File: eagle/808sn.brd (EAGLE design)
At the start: 100 x 80 mm, 76 parts, among them IC1 TL072P, IC2 TL072P, Q1 2N3704, Q45 BC546A, Q46 BC556, Q47 BC546A, Q48 BC546A, Q49 BC546A

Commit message: almost routed
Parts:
- moved C6 124.2 mm to (69.6, 71.4)
- moved C3 90.5 mm to (66.0, 51.1)
- moved C4 89.5 mm to (32.3, 64.5)
- moved C5 75.1 mm to (29.2, 43.7), turned to 270 degrees
- moved LEVEL 65.8 mm to (82.5, 3.56), turned to 0 degrees
- moved TONE 58.0 mm to (51.6, 3.56), turned to 0 degrees
- moved R204 47.6 mm to (67.3, 6.60), turned to 90 degrees
- moved C65 46.4 mm to (55.9, 17.5), turned to 270 degrees
- moved C56 45.3 mm to (55.1, 50.0)
- moved R200 43.2 mm to (51.3, 22.6), turned to 180 degrees
- moved C63 42.6 mm to (36.1, 6.60), turned to 270 degrees
- moved TRIGGER 41.5 mm to (12.2, 34.8)
- moved C68 39.4 mm to (88.4, 17.0), turned to 270 degrees
- moved R180 39.0 mm to (9.91, 31.5)
- moved R196 32.7 mm to (25.1, 36.8), turned to 180 degrees
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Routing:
- net GND: track 0.00 -> 329.1 mm
- net N$12: track 0.00 -> 179.2 mm
- net +12V: track 0.00 -> 115.3 mm
- net N$9: track 0.00 -> 101.1 mm
- net N$35: track 0.00 -> 98.7 mm
- net -12V: track 0.00 -> 85.0 mm
- net N$129: track 0.00 -> 81.4 mm
- net N$707: track 0.00 -> 78.6 mm
- net N$29: track 0.00 -> 64.8 mm
- net N$6: track 0.00 -> 41.4 mm
- net N$27: track 0.00 -> 38.6 mm
- net N$8: track 0.00 -> 37.2 mm
- net N$710: track 0.00 -> 34.2 mm
- net N$26: track 0.00 -> 33.0 mm
- net N$15: track 0.00 -> 32.1 mm
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
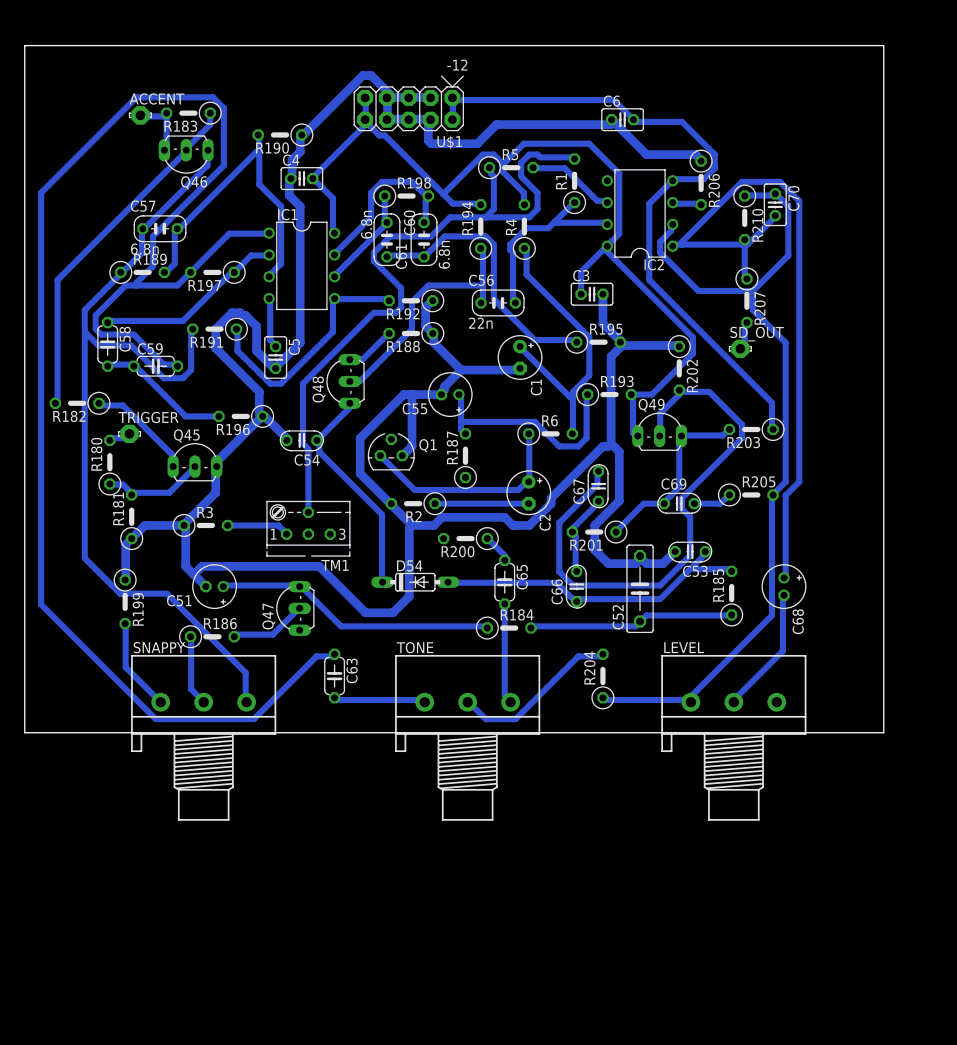
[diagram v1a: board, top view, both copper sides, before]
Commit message: gcode with good separation of traces
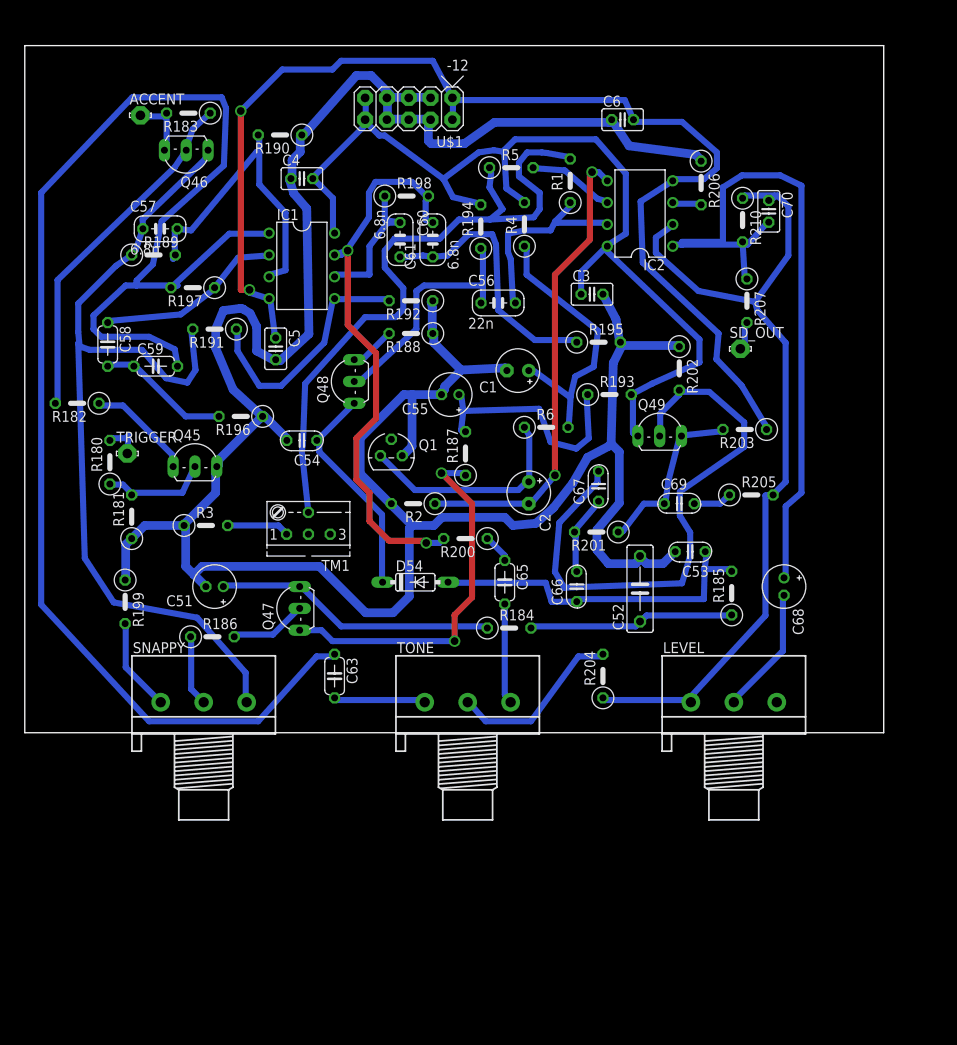
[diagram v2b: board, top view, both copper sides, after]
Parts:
- moved R197 2.90 mm to (19.6, 51.8)
- moved R189 2.40 mm to (15.0, 55.6)
- moved TRIGGER 2.30 mm to (11.9, 32.5)
- moved C1 1.55 mm to (57.4, 42.2), turned to 180 degrees
- moved C60 1.52 mm to (43.7, 57.4)
- moved C70 1.08 mm to (86.6, 60.7)
- moved C5 1.02 mm to (29.2, 44.7)
- moved C61 1.02 mm to (47.5, 57.4)
- moved R6 0.92 mm to (60.7, 35.6)
- moved R203 0.76 mm to (83.8, 35.3)
- moved Q48 0.51 mm to (37.1, 40.9)
- moved R1 0.51 mm to (63.5, 64.3)
- moved R210 0.36 mm to (83.6, 59.7)
- moved R201 0.25 mm to (66.5, 23.4)
- moved R4 0.25 mm to (58.2, 59.2)
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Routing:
- net -12V: track 85.0 -> 140.4 mm, vias 0 -> 2
- net N$14: track 20.1 -> 67.1 mm, vias 0 -> 2
- net N$2: track 10.9 -> 54.8 mm, vias 0 -> 2
- net N$24: track 0.00 -> 43.3 mm, vias 0 -> 2
- net N$160: track 12.1 -> 17.0 mm
- net N$129: track 81.4 -> 85.6 mm
- net N$12: track 179.2 -> 183.1 mm
- net N$29: track 64.8 -> 67.9 mm
- net GND: track 329.1 -> 326.0 mm
- net N$9: track 101.1 -> 104.1 mm
- net N$35: track 98.7 -> 101.2 mm
- net N$27: track 38.6 -> 40.8 mm
- net +12V: track 115.3 -> 117.4 mm
- net SD: track 2.62 -> 4.50 mm
- net N$25: track 26.4 -> 28.2 mm
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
